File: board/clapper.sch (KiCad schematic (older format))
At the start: 22 parts, among them J101 Conn_01x05, J102 AudioJack2, Q101 PN2222A, Q102 PN2222A, SW101 SELECT, SW102 UP, SW104 RESET, SW105 CLAPPER

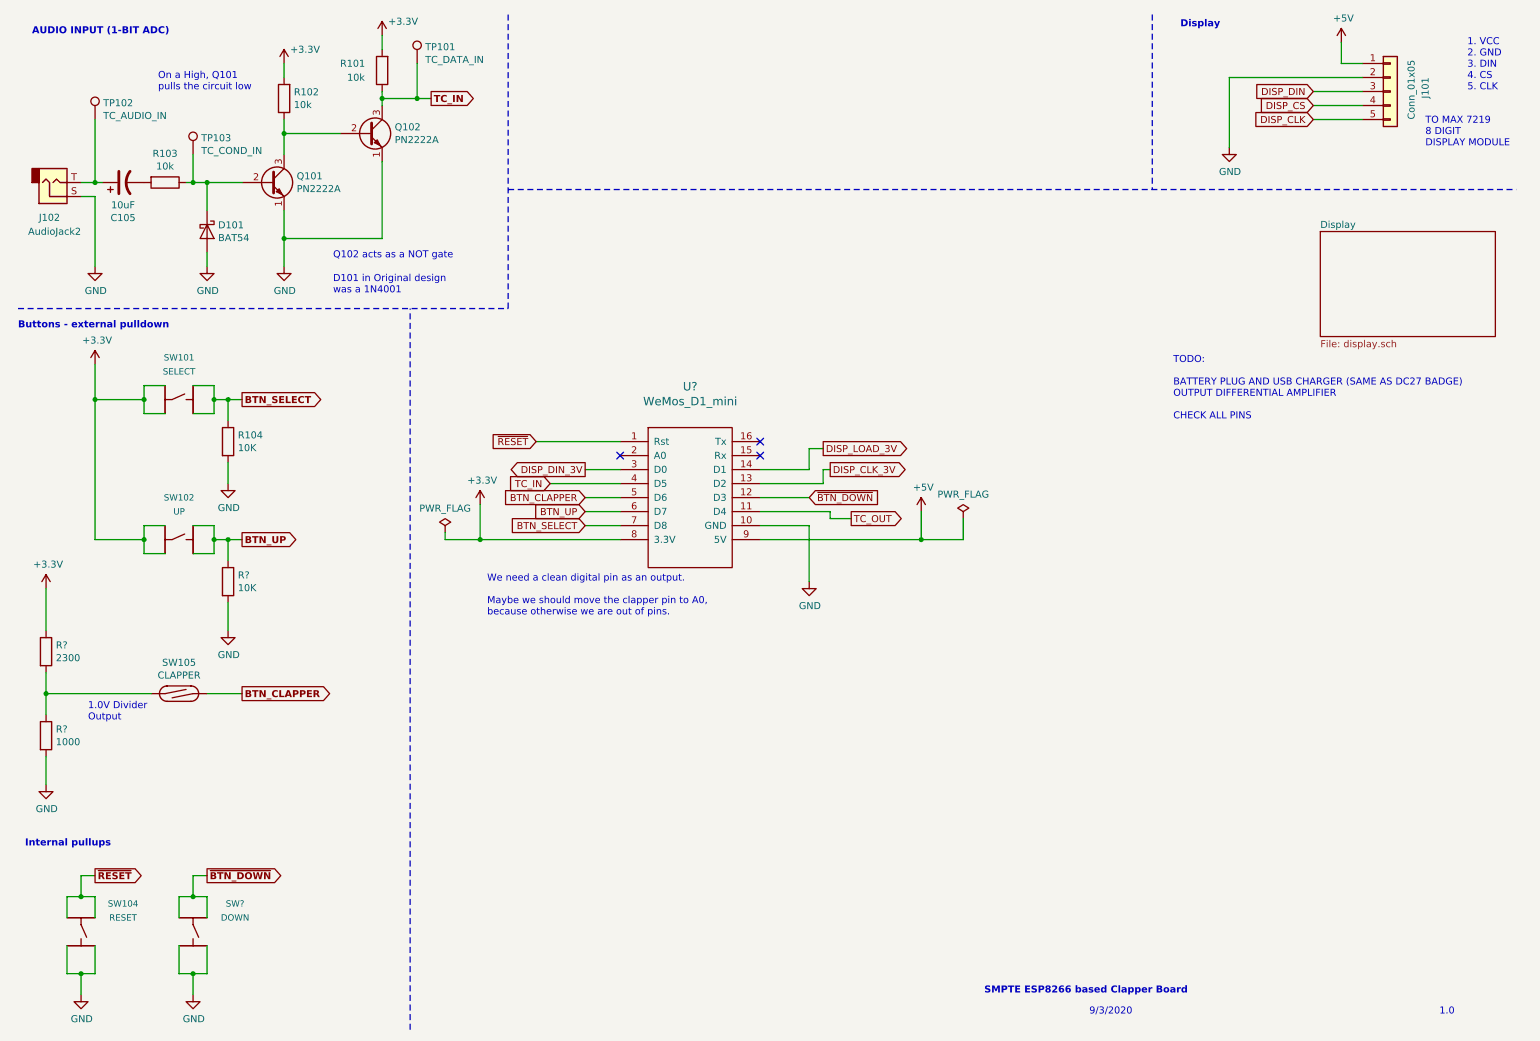
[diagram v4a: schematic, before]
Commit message: add proper analog debouncing
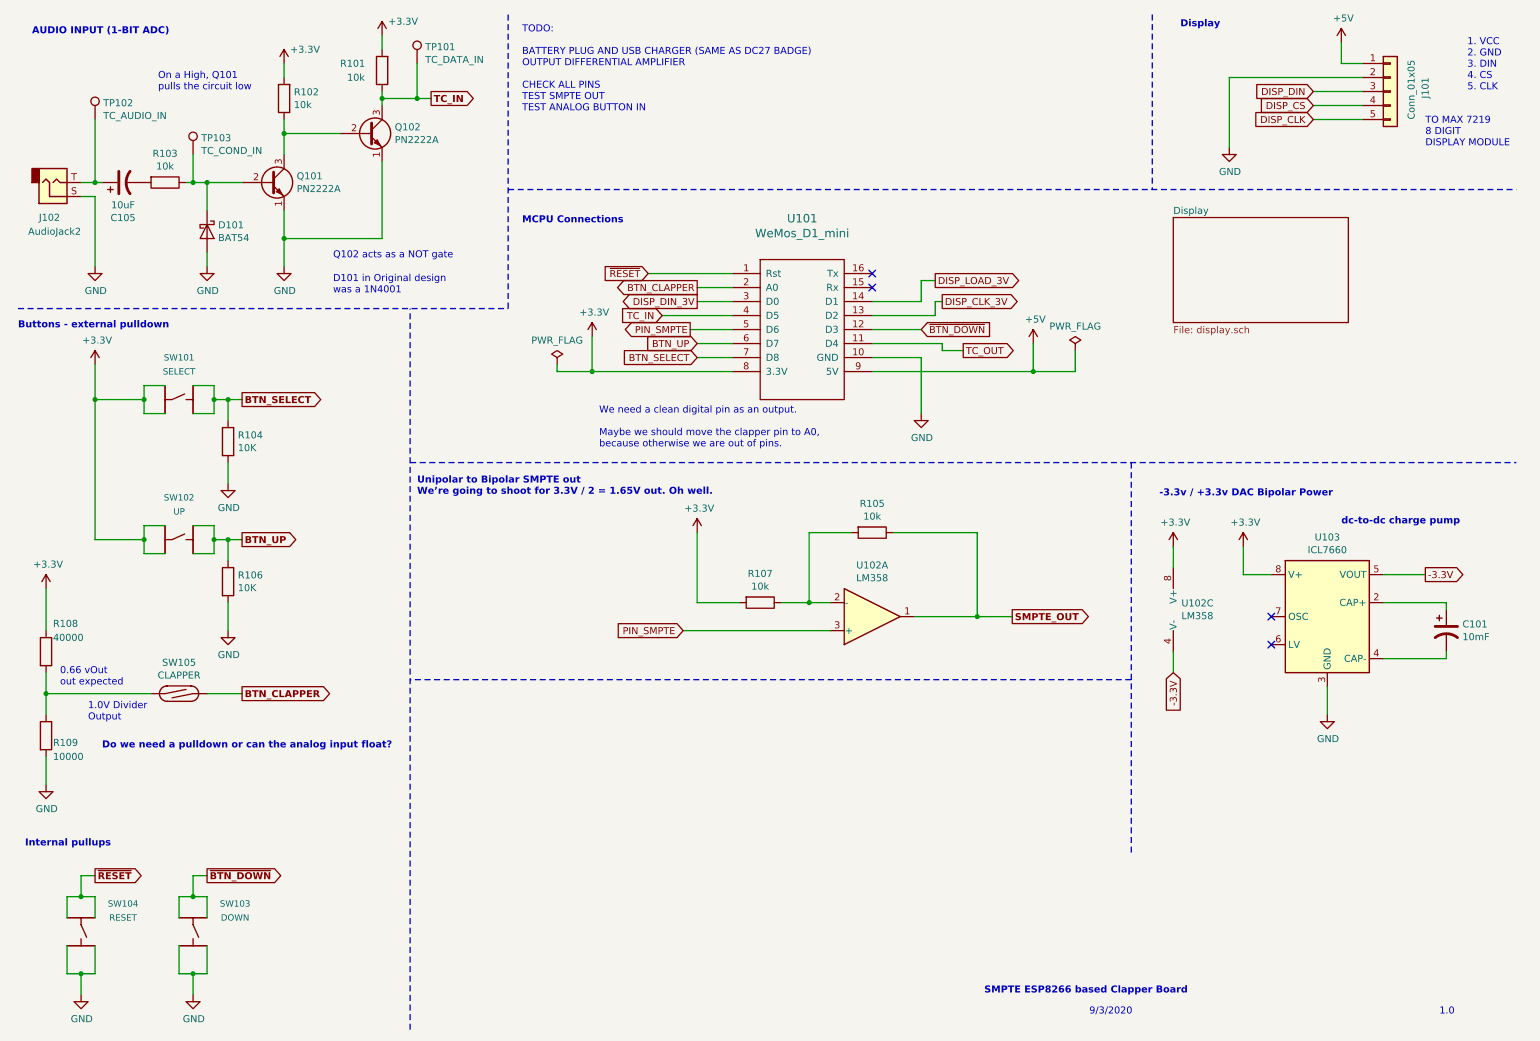
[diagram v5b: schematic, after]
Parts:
- added C101: 10mF, symbol Device:CP1
- added R105, R107: 10k, symbol Device:R
- added U102: LM358, symbol Amplifier_Operational:LM358
- added U103: ICL7660, symbol Regulator_SwitchedCapacitor:ICL7660
- R108: renamed from R?; value 2300 -> 40000
- R109: renamed from R?; value 1000 -> 10000
- gave numbers to parts that had none: 3
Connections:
- net +3V3: now also R107.2, U102.8 (V+), U103.8 (V+)
- net BTN_CLAPPER: now also U101.2 (A0); no longer U101.5 (D6)
- net GND: now also U103.3 (GND)
- new net: R105.2, R107.1, U102.2 (-)
- new net: C101.1, U103.2 (CAP+)
- new net: C101.2, U103.4 (CAP-)
- new net -3.3V: U102.4 (V-), U103.5 (VOUT)
- new net PIN_SMPTE: U101.5 (D6), U102.3 (+)
- new net SMPTE_OUT: R105.1, U102.1
- no-connect marks 3 -> 4
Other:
- note added: "-3.3v / +3.3v DAC Bipolar Power\n"
- note added: "0.66 vOut\nout expected\n"
- note added: "Do we need a pulldown or can the analog input float?"
- note added: "MCPU Connections"
- note added: "TODO:\n\nBATTERY PLUG AND USB CHARGER (SAME AS DC27 BADGE)\nOUTPUT DIFFERENTIAL AMPLIFIER\n\nCHECK ALL PINS\nTEST SMPTE OUT\nTEST ANALOG BUTTON IN\n"
- note added: "Unipolar to Bipolar SMPTE out\nWe’re going to shoot for 3.3V / 2 = 1.65V out. Oh well. \n\n\n"
- note added: "dc-to-dc charge pump\n"
- note removed: "TODO:\n\nBATTERY PLUG AND USB CHARGER (SAME AS DC27 BADGE)\nOUTPUT DIFFERENTIAL AMPLIFIER\n\nCHECK ALL PINS\n"
- moved on the sheet: U101
